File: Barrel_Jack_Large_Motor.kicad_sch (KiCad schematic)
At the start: 23 parts, among them J15 Barrel_Jack, J16 Barrel_Jack, J17 Barrel_Jack, J18 Barrel_Jack, J19 Barrel_Jack, J20 Barrel_Jack, J36 Barrel_Jack, J37 Barrel_Jack, U10 PCF8574ATS, U27 L298N, U28 L298N, U29 L298N, U37 L298N, U38 PCF8574ATS, U39 PCA9685PW

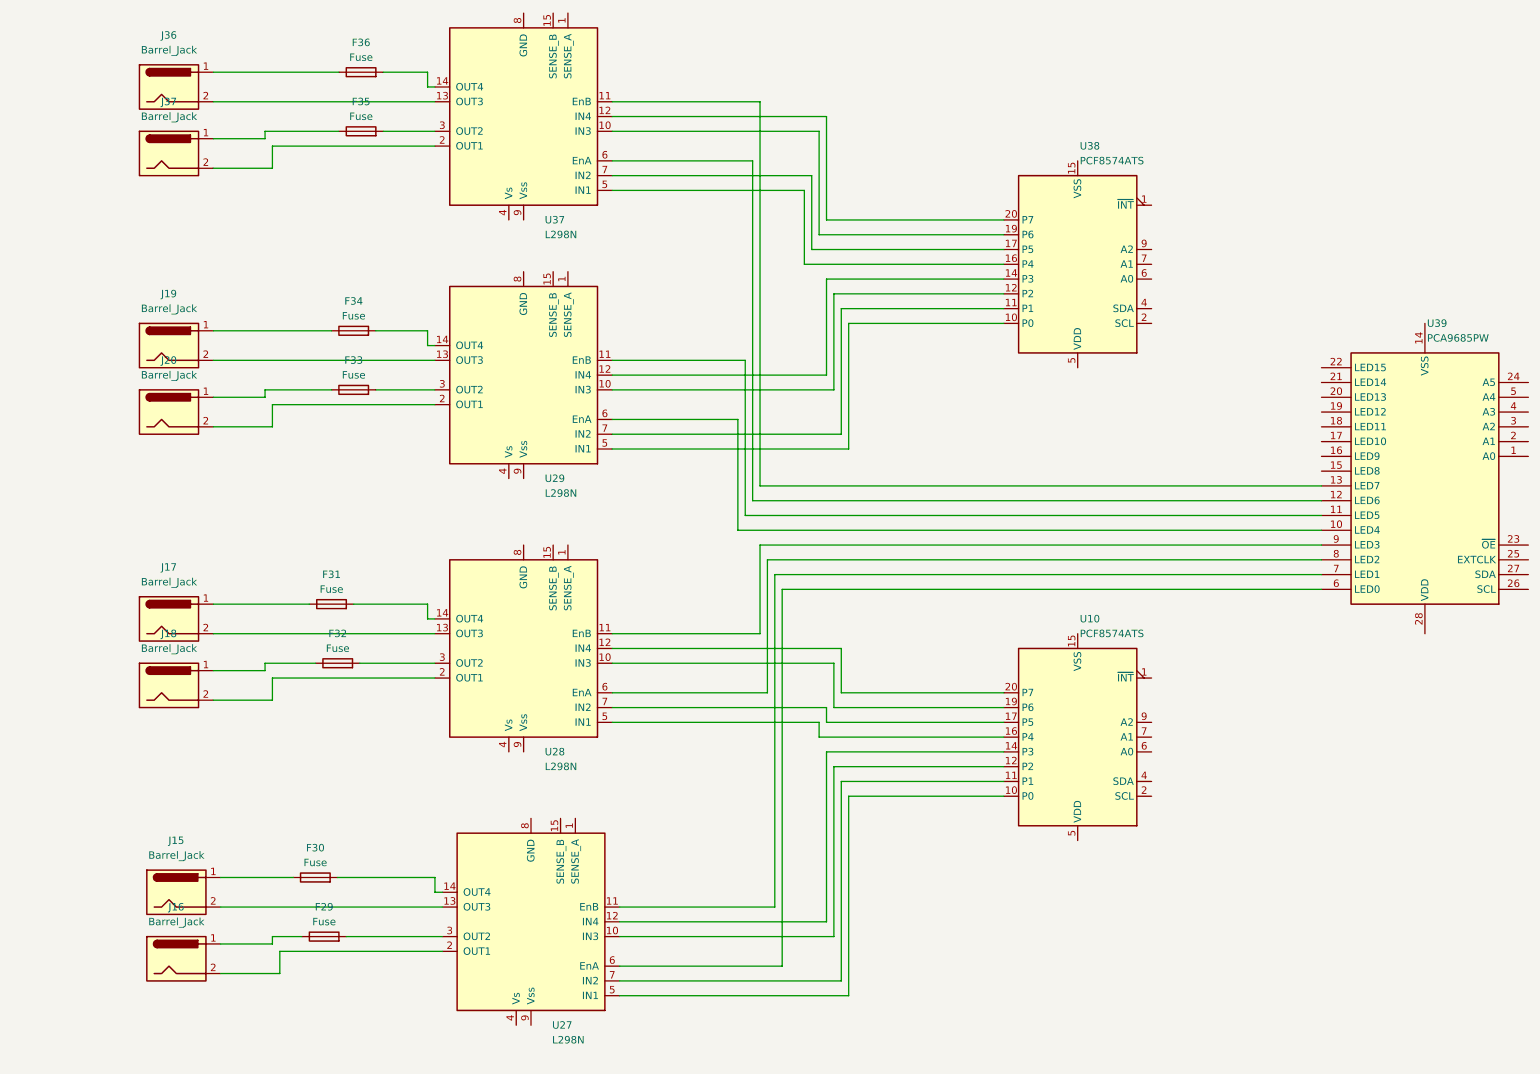
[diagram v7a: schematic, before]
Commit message: added layout from online made room for full 41f switch
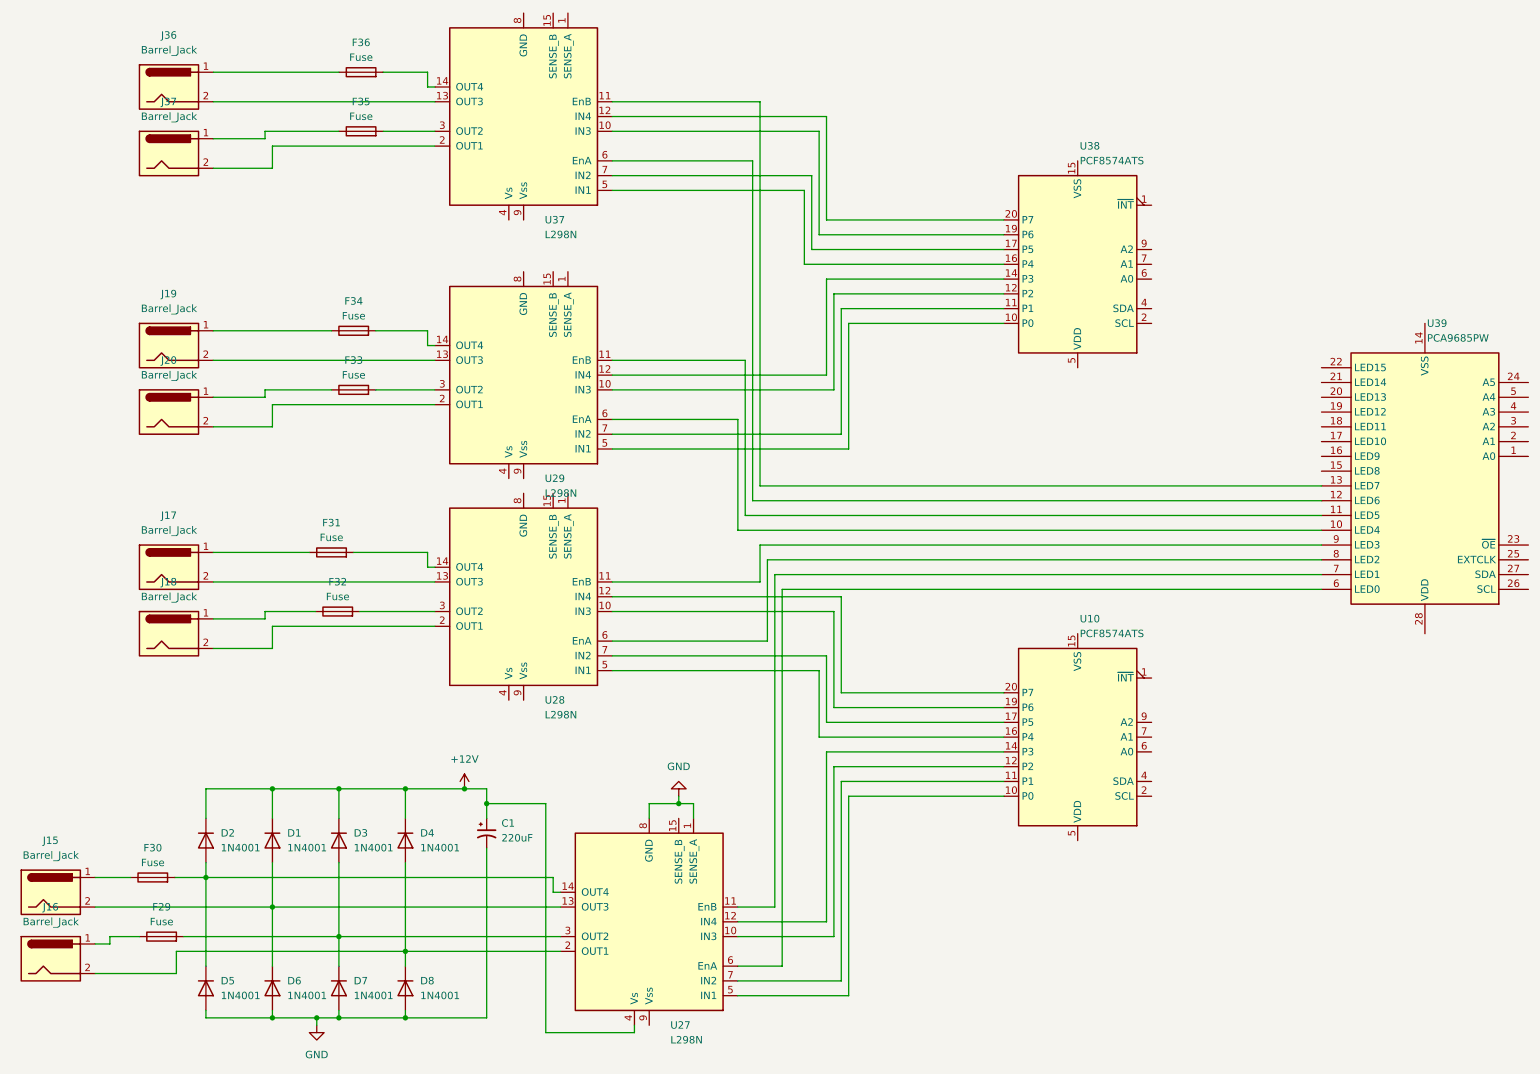
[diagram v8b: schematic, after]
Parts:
- added C1: 220uF, symbol Device:C_Polarized_Small_US
- added D1, D2, D3, D4, D5, D6, D7, D8: 1N4001, Diode_THT:D_DO-41_SOD81_P10.16mm_Horizontal, symbol Diode:1N4001
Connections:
- net at J15.2, U27.13 (OUT3): now also D1.2 (A), D6.1 (K)
- net at F29.2, U27.3 (OUT2): now also D3.2 (A), D7.1 (K)
- net at F30.2, U27.14 (OUT4): now also D2.2 (A), D5.1 (K)
- net at J16.2, U27.2 (OUT1): now also D4.2 (A), D8.1 (K)
- net GND: now reaches U27.1 (SENSE_A)
- net GND: now also U27.8 (GND), C1.2, D5.2 (A), D6.2 (A), D7.2 (A), D8.2 (A)
- net +12V: now reaches U27.4 (Vs)
- net +12V: now also C1.1, D1.1 (K), D2.1 (K), D3.1 (K), D4.1 (K)
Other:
- moved on the sheet: F29, F30, F31, F32, J15, J16, J17, J18, U27, U28
